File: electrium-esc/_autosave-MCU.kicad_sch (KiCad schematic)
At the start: 23 parts

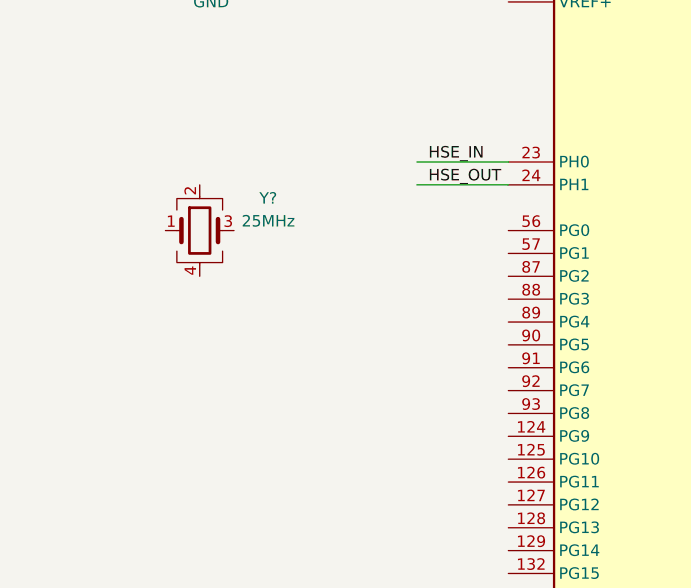
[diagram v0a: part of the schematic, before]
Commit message: Add further connections to MCU
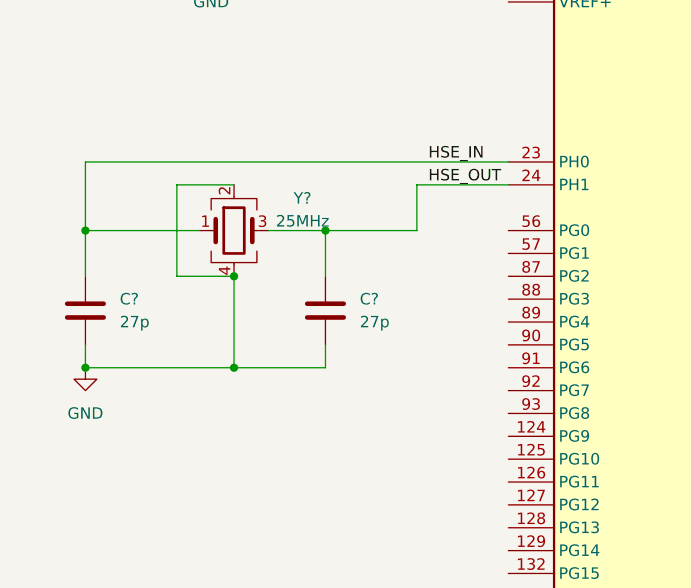
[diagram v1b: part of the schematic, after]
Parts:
- added C? (x2): 27p, symbol Device:C
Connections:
- net GND: now also Y?.2, Y?.4, C?.2, C?.2
- net HSE_IN: now also Y?.1, C?.1
- net HSE_OUT: now also Y?.3, C?.1
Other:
- moved on the sheet: Y?
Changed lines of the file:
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@@
   (junction (at 187.96 40.64) (diameter 0) (color 0 0 0 0)
   )
+  (junction (at 26.67 120.65) (diameter 0) (color 0 0 0 0)
+  )
+  (junction (at 43.18 120.65) (diameter 0) (color 0 0 0 0)
+  )
   (junction (at 91.44 53.34) (diameter 0) (color 0 0 0 0)
   )
@@
   (junction (at 165.1 40.64) (diameter 0) (color 0 0 0 0)
   )
+  (junction (at 43.18 110.49) (diameter 0) (color 0 0 0 0)
+  )
   (junction (at 116.84 53.34) (diameter 0) (color 0 0 0 0)
   )
@@
   (junction (at 109.22 238.76) (diameter 0) (color 0 0 0 0)
   )
+  (junction (at 53.34 105.41) (diameter 0) (color 0 0 0 0)
+  )
   (junction (at 176.53 20.32) (diameter 0) (color 0 0 0 0)
   )
@@
   (junction (at 99.06 238.76) (diameter 0) (color 0 0 0 0)
   )
+  (junction (at 26.67 105.41) (diameter 0) (color 0 0 0 0)
+  )
   (junction (at 106.68 53.34) (diameter 0) (color 0 0 0 0)
   )
@@
     (stroke (width 0) (type default) (color 0 0 0 0))
   )
+  (wire (pts (xy 46.99 105.41) (xy 53.34 105.41))
+    (stroke (width 0) (type default) (color 0 0 0 0))
+  )
+  (wire (pts (xy 26.67 105.41) (xy 26.67 110.49))
+    (stroke (width 0) (type default) (color 0 0 0 0))
+  )
   (wire (pts (xy 116.84 53.34) (xy 119.38 53.34))
     (stroke (width 0) (type default) (color 0 0 0 0))
@@
     (stroke (width 0) (type default) (color 0 0 0 0))
   )
-  (wire (pts (xy 63.5 97.79) (xy 73.66 97.79))
+  (wire (pts (xy 26.67 97.79) (xy 73.66 97.79))
     (stroke (width 0) (type default) (color 0 0 0 0))
   )
@@
     (stroke (width 0) (type default) (color 0 0 0 0))
   )
+  (wire (pts (xy 26.67 120.65) (xy 43.18 120.65))
+    (stroke (width 0) (type default) (color 0 0 0 0))
+  )
   (wire (pts (xy 135.89 33.02) (xy 135.89 44.45))
     (stroke (width 0) (type default) (color 0 0 0 0))
@@
     (stroke (width 0) (type default) (color 0 0 0 0))
   )
+  (wire (pts (xy 53.34 105.41) (xy 53.34 110.49))
+    (stroke (width 0) (type default) (color 0 0 0 0))
+  )
   (wire (pts (xy 99.06 237.49) (xy 99.06 238.76))
     (stroke (width 0) (type default) (color 0 0 0 0))
@@
     (stroke (width 0) (type default) (color 0 0 0 0))
   )
+  (wire (pts (xy 36.83 110.49) (xy 43.18 110.49))
+    (stroke (width 0) (type default) (color 0 0 0 0))
+  )
   (wire (pts (xy 165.1 27.94) (xy 176.53 27.94))
     (stroke (width 0) (type default) (color 0 0 0 0))
@@
     (stroke (width 0) (type default) (color 0 0 0 0))
   )
+  (wire (pts (xy 63.5 105.41) (xy 63.5 100.33))
+    (stroke (width 0) (type default) (color 0 0 0 0))
+  )
   (wire (pts (xy 88.9 53.34) (xy 88.9 54.61))
     (stroke (width 0) (type default) (color 0 0 0 0))
@@
     (stroke (width 0) (type default) (color 0 0 0 0))
   )
+  (wire (pts (xy 43.18 120.65) (xy 53.34 120.65))
+    (stroke (width 0) (type default) (color 0 0 0 0))
+  )
   (wire (pts (xy 176.53 40.64) (xy 187.96 40.64))
     (stroke (width 0) (type default) (color 0 0 0 0))
@@
     (stroke (width 0) (type default) (color 0 0 0 0))
   )
+  (wire (pts (xy 26.67 105.41) (xy 39.37 105.41))
+    (stroke (width 0) (type default) (color 0 0 0 0))
+  )
   (wire (pts (xy 176.53 52.07) (xy 187.96 52.07))
     (stroke (width 0) (type default) (color 0 0 0 0))
@@
     (stroke (width 0) (type default) (color 0 0 0 0))
   )
+  (wire (pts (xy 26.67 97.79) (xy 26.67 105.41))
+    (stroke (width 0) (type default) (color 0 0 0 0))
+  )
   (wire (pts (xy 153.67 52.07) (xy 165.1 52.07))
     (stroke (width 0) (type default) (color 0 0 0 0))
@@
     (stroke (width 0) (type default) (color 0 0 0 0))
   )
+  (wire (pts (xy 36.83 100.33) (xy 36.83 110.49))
+    (stroke (width 0) (type default) (color 0 0 0 0))
+  )
   (wire (pts (xy 104.14 53.34) (xy 104.14 54.61))
     (stroke (width 0) (type default) (color 0 0 0 0))
@@
     (stroke (width 0) (type default) (color 0 0 0 0))
   )
+  (wire (pts (xy 53.34 120.65) (xy 53.34 118.11))
+    (stroke (width 0) (type default) (color 0 0 0 0))
+  )
   (wire (pts (xy 135.89 44.45) (xy 142.24 44.45))
     (stroke (width 0) (type default) (color 0 0 0 0))
   )
+  (wire (pts (xy 43.18 110.49) (xy 43.18 120.65))
+    (stroke (width 0) (type default) (color 0 0 0 0))
+  )
   (wire (pts (xy 153.67 27.94) (xy 165.1 27.94))
     (stroke (width 0) (type default) (color 0 0 0 0))
@@
     (stroke (width 0) (type default) (color 0 0 0 0))
   )
+  (wire (pts (xy 53.34 105.41) (xy 63.5 105.41))
+    (stroke (width 0) (type default) (color 0 0 0 0))
+  )
   (wire (pts (xy 165.1 52.07) (xy 176.53 52.07))
     (stroke (width 0) (type default) (color 0 0 0 0))
@@
     (stroke (width 0) (type default) (color 0 0 0 0))
   )
+  (wire (pts (xy 43.18 100.33) (xy 36.83 100.33))
+    (stroke (width 0) (type default) (color 0 0 0 0))
+  )
   (wire (pts (xy 176.53 33.02) (xy 187.96 33.02))
     (stroke (width 0) (type default) (color 0 0 0 0))
   )
   (wire (pts (xy 93.98 238.76) (xy 96.52 238.76))
+    (stroke (width 0) (type default) (color 0 0 0 0))
+  )
+  (wire (pts (xy 26.67 120.65) (xy 26.67 118.11))
     (stroke (width 0) (type default) (color 0 0 0 0))
   )
@@
     )
     (property "Datasheet" "" (id 3) (at 81.28 35.56 0)
+      (effects (font (size 1.27 1.27)) hide)
+    )
+    (pin "1")
+  )
+  (symbol (lib_id "power:GND") (at 26.67 120.65 0) (unit 1)
+    (in_bom yes) (on_board yes) (fields_autoplaced)
+    (property "Reference" "#PWR?" (id 0) (at 26.67 127 0)
+      (effects (font (size 1.27 1.27)) hide)
+    )
+    (property "Value" "GND" (id 1) (at 26.67 125.73 0))
+    (property "Footprint" "" (id 2) (at 26.67 120.65 0)
+      (effects (font (size 1.27 1.27)) hide)
+    )
+    (property "Datasheet" "" (id 3) (at 26.67 120.65 0)
       (effects (font (size 1.27 1.27)) hide)
     )
@@
     (pin "2")
   )
-  (symbol (lib_id "Device:Crystal_GND24") (at 39.37 105.41 0) (unit 1)
-    (in_bom yes) (on_board yes) (fields_autoplaced)
-    (property "Reference" "Y?" (id 0) (at 46.99 101.8286 0))
-    (property "Value" "25MHz" (id 1) (at 46.99 104.3686 0))
-    (property "Footprint" "" (id 2) (at 39.37 105.41 0)
-      (effects (font (size 1.27 1.27)) hide)
-    )
-    (property "Datasheet" "~" (id 3) (at 39.37 105.41 0)
+  (symbol (lib_id "Device:Crystal_GND24") (at 43.18 105.41 0) (unit 1)
+    (in_bom yes) (on_board yes) (fields_autoplaced)
+    (property "Reference" "Y?" (id 0) (at 50.8 101.8286 0))
+    (property "Value" "25MHz" (id 1) (at 50.8 104.3686 0))
+    (property "Footprint" "" (id 2) (at 43.18 105.41 0)
+      (effects (font (size 1.27 1.27)) hide)
+    )
+    (property "Datasheet" "~" (id 3) (at 43.18 105.41 0)
       (effects (font (size 1.27 1.27)) hide)
     )
@@
     (pin "2")
   )
+  (symbol (lib_id "Device:C") (at 53.34 114.3 0) (unit 1)
+    (in_bom yes) (on_board yes) (fields_autoplaced)
+    (property "Reference" "C?" (id 0) (at 57.15 113.0299 0)
+      (effects (font (size 1.27 1.27)) (justify left))
+    )
+    (property "Value" "27p" (id 1) (at 57.15 115.5699 0)
+      (effects (font (size 1.27 1.27)) (justify left))
+    )
+    (property "Footprint" "" (id 2) (at 54.3052 118.11 0)
+      (effects (font (size 1.27 1.27)) hide)
+    )
+    (property "Datasheet" "~" (id 3) (at 53.34 114.3 0)
+      (effects (font (size 1.27 1.27)) hide)
+    )
+    (pin "1")
+    (pin "2")
+  )
   (symbol (lib_id "Device:C") (at 176.53 24.13 0) (unit 1)
     (in_bom yes) (on_board yes) (fields_autoplaced)
@@
       (effects (font (size 1.27 1.27)) hide)
     )
+    (pin "1")
+    (pin "2")
+  )
+  (symbol (lib_id "Device:C") (at 26.67 114.3 0) (unit 1)
+    (in_bom yes) (on_board yes) (fields_autoplaced)
+    (property "Reference" "C?" (id 0) (at 30.48 113.0299 0)
+      (effects (font (size 1.27 1.27)) (justify left))
+    )
+    (property "Value" "27p" (id 1) (at 30.48 115.5699 0)
+      (effects (font (size 1.27 1.27)) (justify left))
+    )
+    (property "Footprint" "" (id 2) (at 27.6352 118.11 0)
+      (effects (font (size 1.27 1.27)) hide)
+    )
+    (property "Datasheet" "~" (id 3) (at 26.67 114.3 0)
+      (effects (font (size 1.27 1.27)) hide)
+    )
